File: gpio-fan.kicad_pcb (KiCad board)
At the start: 2 copper layers, 36 x 21.7 mm, 26 parts, among them J1 Conn_01x05, J2 Conn_01x05, J3 Conn_01x02, J4 Conn_02x07_Odd_Even, J5 Conn_01x03, J6 Conn_01x02, J7 Conn_01x02, J8 Conn_01x02, Q1 BSS214NW, SW1 SW_DIP_x03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

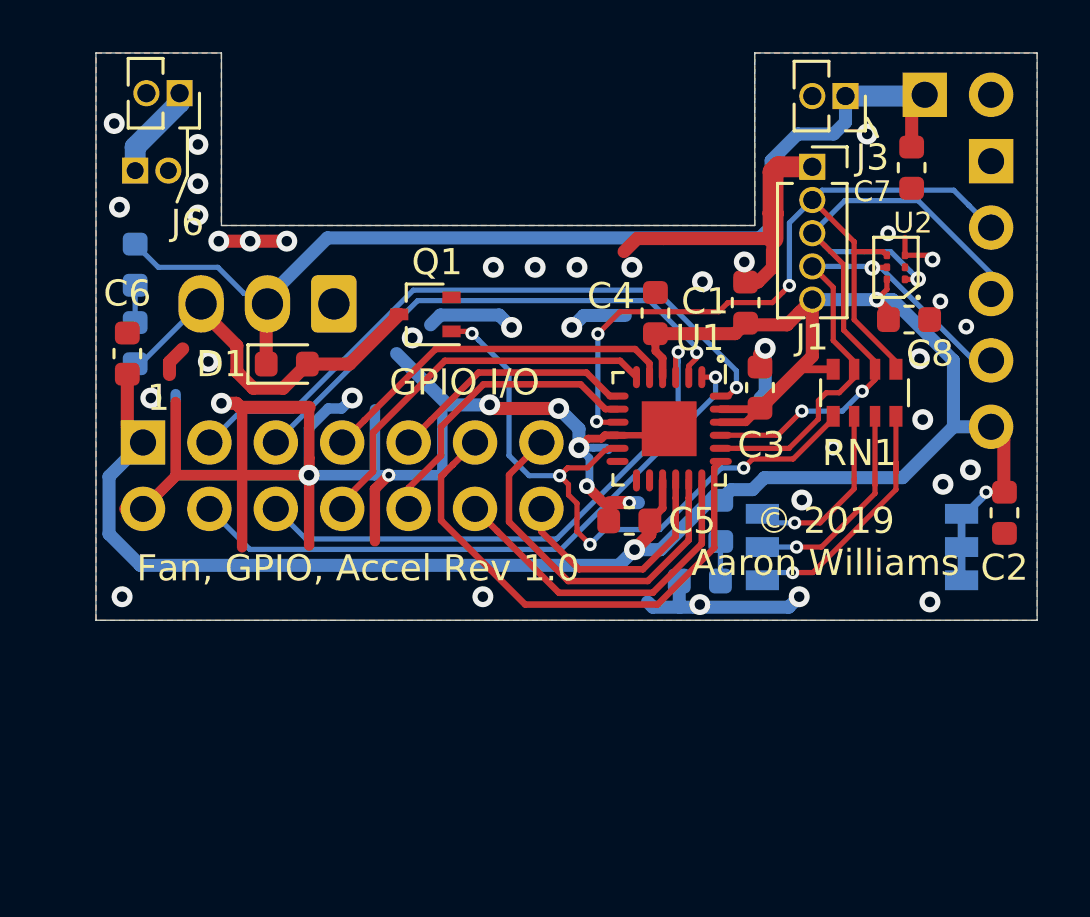
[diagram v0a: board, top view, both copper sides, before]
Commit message: Added large via to match 3.8, minor changes
Signed-off-by: Aaron Williams <aaron.w2@gmail.com>
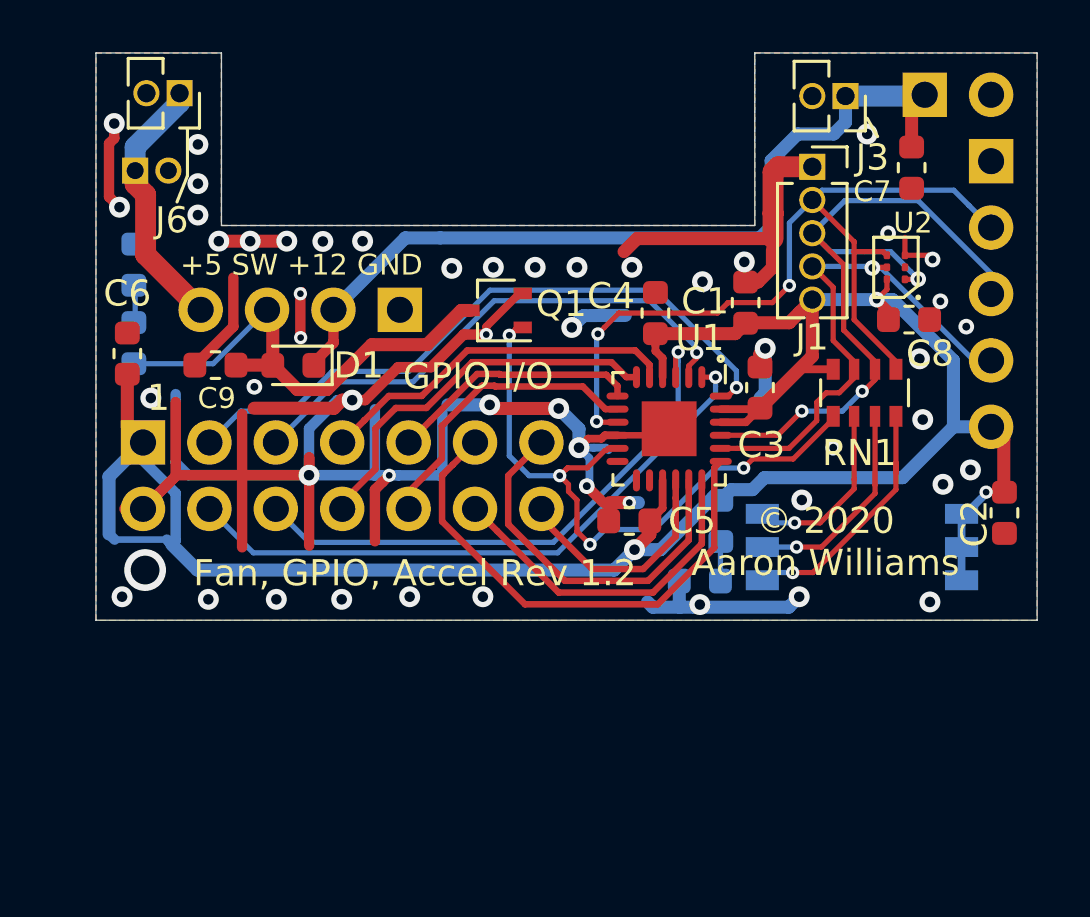
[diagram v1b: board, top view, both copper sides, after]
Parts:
- added C9: 1uF, Capacitor_SMD:C_0603_1608Metric, F.Cu at (54.6, 53.9)
- J5: value Conn_01x03 -> Conn_01x04_Male; footprint Connector_Molex:Molex_KK-254_AE-6410-03A_1x03_P2.54mm_Vertical -> Connector_PinHeader_2.54mm:PinHeader_1x04_P2.54mm_Vertical
- R1: value 4.7K -> 1K
- moved Q1 2.73 mm to (65.3, 51.9)
- moved J5 2.54 mm to (61.6, 51.8), turned to 90 degrees
- moved D1 0.25 mm to (57.5, 54.0), turned to 180 degrees
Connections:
- R1 pad 1: +12V -> +5V
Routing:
- net +5V: track 3.66 -> 13.7 mm
- net +12V: track 41.2 -> 33.0 mm
- net GND: track 105.3 -> 112.1 mm, vias 45 -> 53
- net +3V3: track 82.7 -> 87.3 mm
- net /FET: track 14.5 -> 18.8 mm
- net /FAN_CTL: track 25.5 -> 24.6 mm
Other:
- board text added: "+5 SW +12 GND"
- board text added: "Fan, GPIO, Accel Rev 1.2"
- board text added: "GND +12 SW +5"
- board text added: "J5: GND +12V FET +5"
- board text added: "© 2020 Aaron Williams"
- board text removed: "Fan, GPIO, Accel Rev 1.0"
- board text removed: "J5: GND +12V FET"
- board text removed: "© 2019 Aaron Williams"

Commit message: Upgraded to revision 1.3, changed temperature sensor and accelerometer.
This now uses a combined part that should be a lot easier to solder.
The new ST part also includes a temperature sensor and it is supported
by the Arduino library.

Signed-off-by: Aaron Williams <aaron.w2@gmail.com>
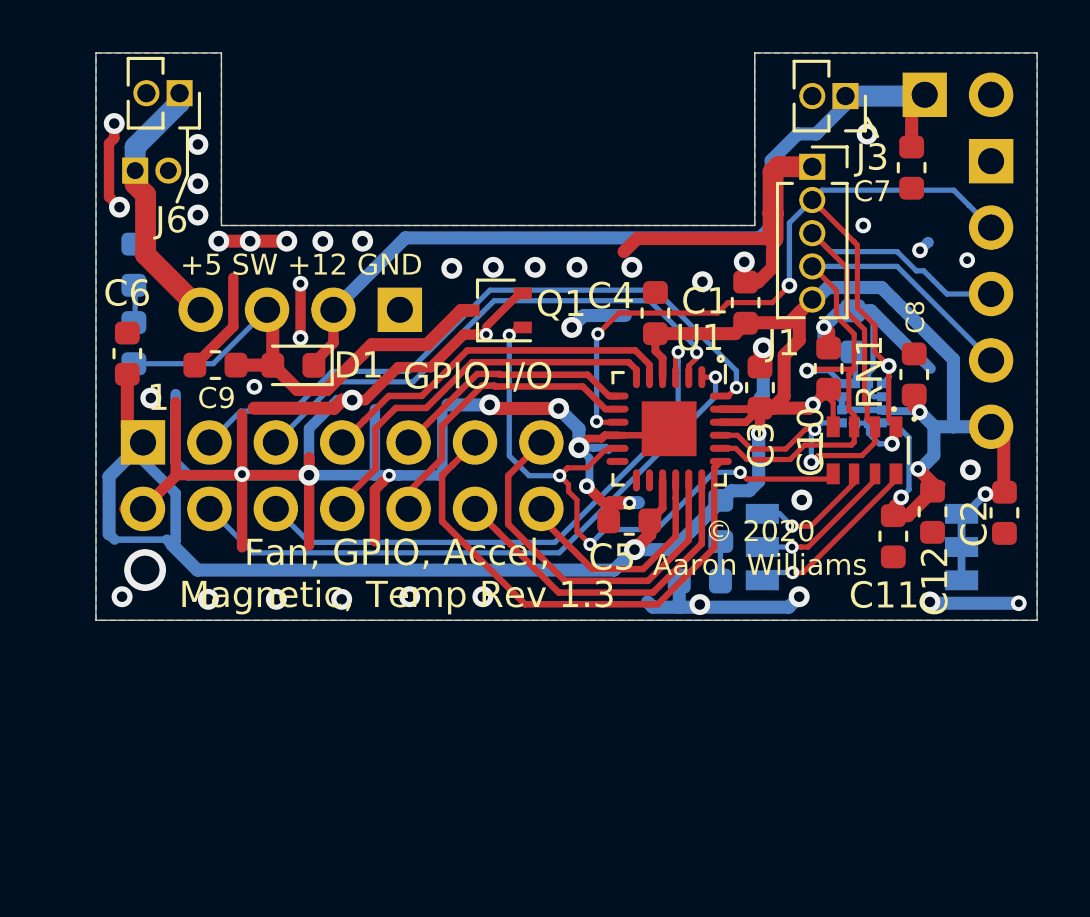
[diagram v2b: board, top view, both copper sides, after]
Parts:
- added C10: 0.22uF, Capacitor_SMD:C_0603_1608Metric, B.Cu at (79.0, 52.6)
- added C10: 0.01uF, Capacitor_SMD:C_0603_1608Metric, F.Cu at (78.0, 54.1)
- added C11: 0.1uF, Capacitor_SMD:C_0603_1608Metric, F.Cu at (80.5, 60.5)
- added C12: 10uF, Capacitor_SMD:C_0603_1608Metric, F.Cu at (82.0, 59.5)
- C8: value 1uF -> 0.1uF
- J2: value Conn_01x05 -> Conn_01x05 DNS
- J7, J8: value Conn_01x02 -> Conn_01x02 DNS
- U2: value MXC400XXC -> LSM303AGRTR; footprint Aaron:MXC400XXC -> Package_LGA:LGA-12_2x2mm_P0.5mm; moved to B.Cu
- moved U2 5.36 mm to (79.3, 55.4), turned to 0 degrees
- moved RN1 2.20 mm to (79.4, 57.2)
- moved C8 2.11 mm to (81.3, 54.3), turned to 90 degrees
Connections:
- U2 pad 2: Net-(U2-Pad2) -> +3V3
- U2 pad 3: GND -> +3V3
- U2 pad 4: /~INT -> /SDA
- U2 pad 5: /SDA -> Net-(C10-Pad1)
- U2 pad 6: +3V3 -> GND
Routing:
- net GND: track 112.1 -> 125.8 mm, vias 53 -> 51
- net +3V3: track 87.3 -> 99.0 mm, vias 3 -> 7
- net /SDA: track 20.4 -> 25.0 mm
- net /~INT: track 32.6 -> 37.0 mm, vias 3 -> 5
- net /~INT_PU: track 9.88 -> 6.93 mm
- net /SDA_PU: track 8.11 -> 5.61 mm
- net /SCL_PU: track 6.97 -> 4.74 mm
- net /SCL: track 28.0 -> 26.1 mm, vias 3 -> 2
- net Net-(C10-Pad1): track 0.00 -> 1.24 mm
- net /FAN_CTL: track 24.6 -> 23.9 mm
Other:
- board text added: "Fan, GPIO, Accel, Magnetic, Temp Rev 1.3"
- board text added: "GND ~INT~ SCL SDA 3"
- board text added: "I2C TERM"
- board text removed: "Fan, GPIO, Accel Rev 1.2"
- board text removed: "GND ~INT~ SCL SDA 3.3V"

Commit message: Fixed mislabeled capacitor and other minor changes.
Signed-off-by: Aaron Williams <aaron.w2@gmail.com>
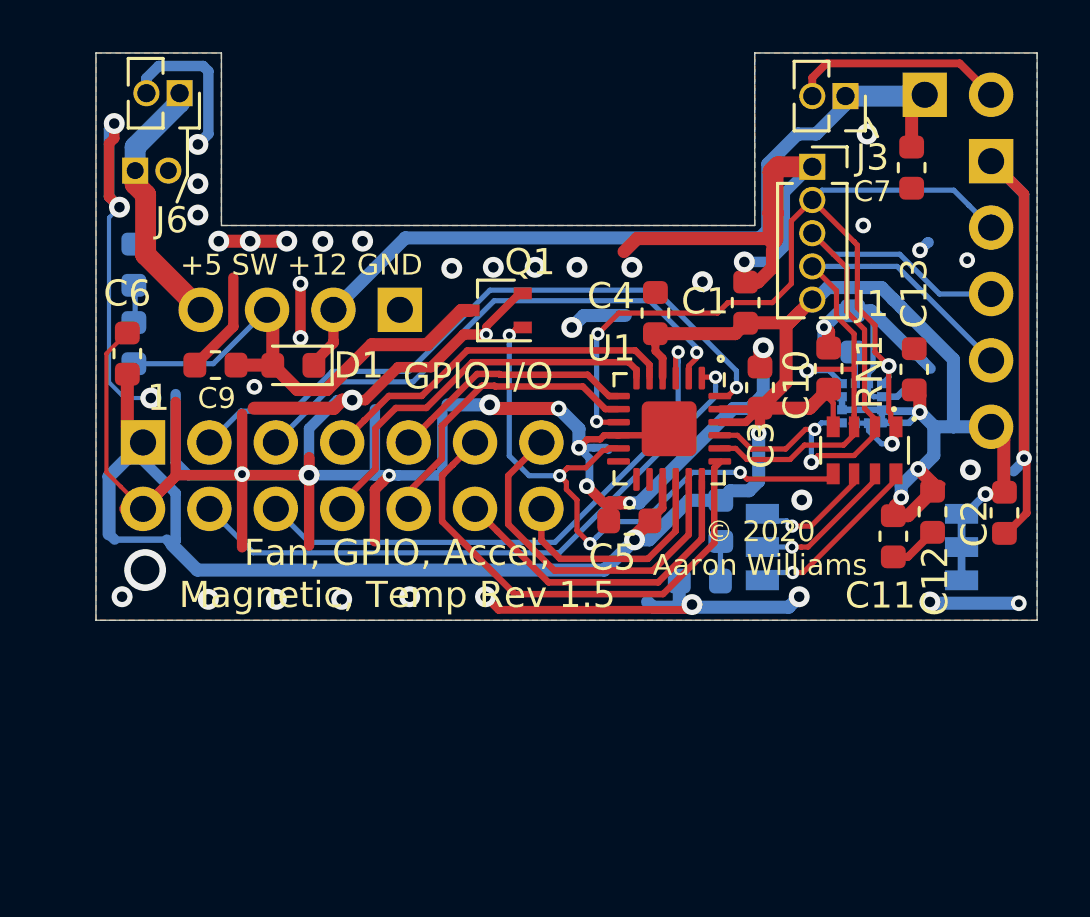
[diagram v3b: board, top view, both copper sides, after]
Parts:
- U1: footprint Aaron:HWQFN-24_EP_4x4_Pitch0.5mm -> Package_DFN_QFN:Texas_S-PVQFN-N24_EP2.1x2.1mm
- moved C13 0.20 mm to (81.3, 54.1)
- renumbered C8 to C13
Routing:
- net GND: track 125.8 -> 210.5 mm, vias 51 -> 52
- net +3V3: track 99.0 -> 98.4 mm, vias 7 -> 6
- net /~INT: vias 5 -> 4
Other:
- board text added: "Fan, GPIO, Accel, Magnetic, Temp Rev 1.5"
- board text removed: "Fan, GPIO, Accel, Magnetic, Temp Rev 1.3"

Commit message: Fixed J6, dimmed LEDs, and added ADC for light sensor
This also expands the board size where the switches are so that it can be
better mounted to the main board via the +5V pins near the speaker connector.

Signed-off-by: Aaron Williams <aaron.w2@gmail.com>
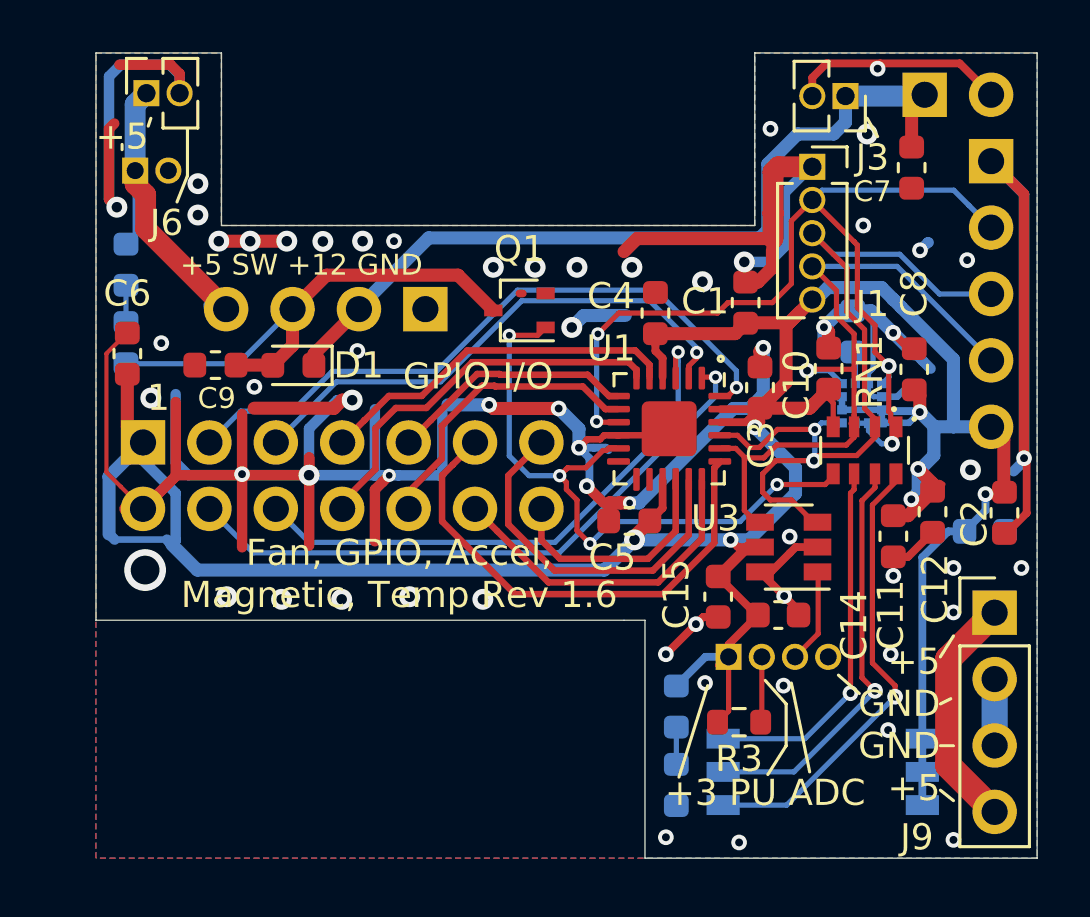
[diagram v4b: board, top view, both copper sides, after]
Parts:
- added C13: 0.1uF, Capacitor_SMD:C_0603_1608Metric, B.Cu at (84.0, 60.3)
- added C14: 1uF, Capacitor_SMD:C_0603_1608Metric, F.Cu at (76.1, 63.5)
- added C15: 0.1uF, Capacitor_SMD:C_0603_1608Metric, F.Cu at (73.8, 62.8)
- added J10: Conn_01x04 DNS, Connector_PinHeader_1.27mm:PinHeader_1x04_P1.27mm_Vertical, B.Cu at (74.2, 65.1)
- added J9: Conn_01x04 DNS, Connector_PinHeader_2.54mm:PinHeader_1x04_P2.54mm_Vertical, F.Cu at (84.4, 63.4)
- added R3: 4.7K, Resistor_SMD:R_0603_1608Metric, F.Cu at (74.6, 67.6)
- added U3: ADS1110, Package_TO_SOT_SMD:SOT-23-6, F.Cu at (76.5, 60.9)
- J5: value Conn_01x04_Male -> Conn_01x04 DNS
- R2: value 33 -> 100
- moved SW1 8.73 mm to (77.8, 69.5)
- moved D3 7.85 mm to (72.2, 70.0), turned to 90 degrees
- moved R2 7.30 mm to (72.2, 67.0)
- moved J6 1.27 mm to (51.9, 43.5), turned to 90 degrees
- moved J5 0.98 mm to (62.6, 51.8)
- moved Q1 0.88 mm to (66.2, 51.9)
- moved D2 0.30 mm to (51.1, 53.1)
- moved R1 0.30 mm to (51.1, 50.1)
- renumbered C13 to C8
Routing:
- net GND: track 210.5 -> 182.3 mm, vias 52 -> 61
- net +3V3: track 98.4 -> 123.8 mm, vias 6 -> 7
- net /~INT_PU: track 6.93 -> 17.6 mm
- net /SDA_PU: track 5.61 -> 15.8 mm
- net /SCL_PU: track 4.74 -> 14.0 mm
- net Net-(J9-Pad1): track 0.00 -> 9.09 mm
- net /SCL: track 26.0 -> 31.2 mm
- net /ADC_IN: track 0.00 -> 3.63 mm
- net /SDA: track 24.7 -> 27.5 mm
- net /PU_OUT: track 0.00 -> 2.52 mm
- net /FET: track 18.8 -> 19.9 mm
- net +5V: track 13.7 -> 12.9 mm
- net /FAN_CTL: track 23.8 -> 24.6 mm
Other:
- board size 36 x 21.7 mm -> 36 x 30.8 mm
- board text added: "+3 PU ADC"
- board text added: "+3 PU ADC GND"
- board text added: "+5"
- board text added: "+5 GND GND +5"
- board text added: "3 G"
- board text added: "Fan, GPIO, Accel, Magnetic, Temp Rev 1.6"
- board text removed: "Fan, GPIO, Accel, Magnetic, Temp Rev 1.5"

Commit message: Made minimum via hole size 0.3mm.
Signed-off-by: Aaron Williams <aaron.w2@gmail.com>
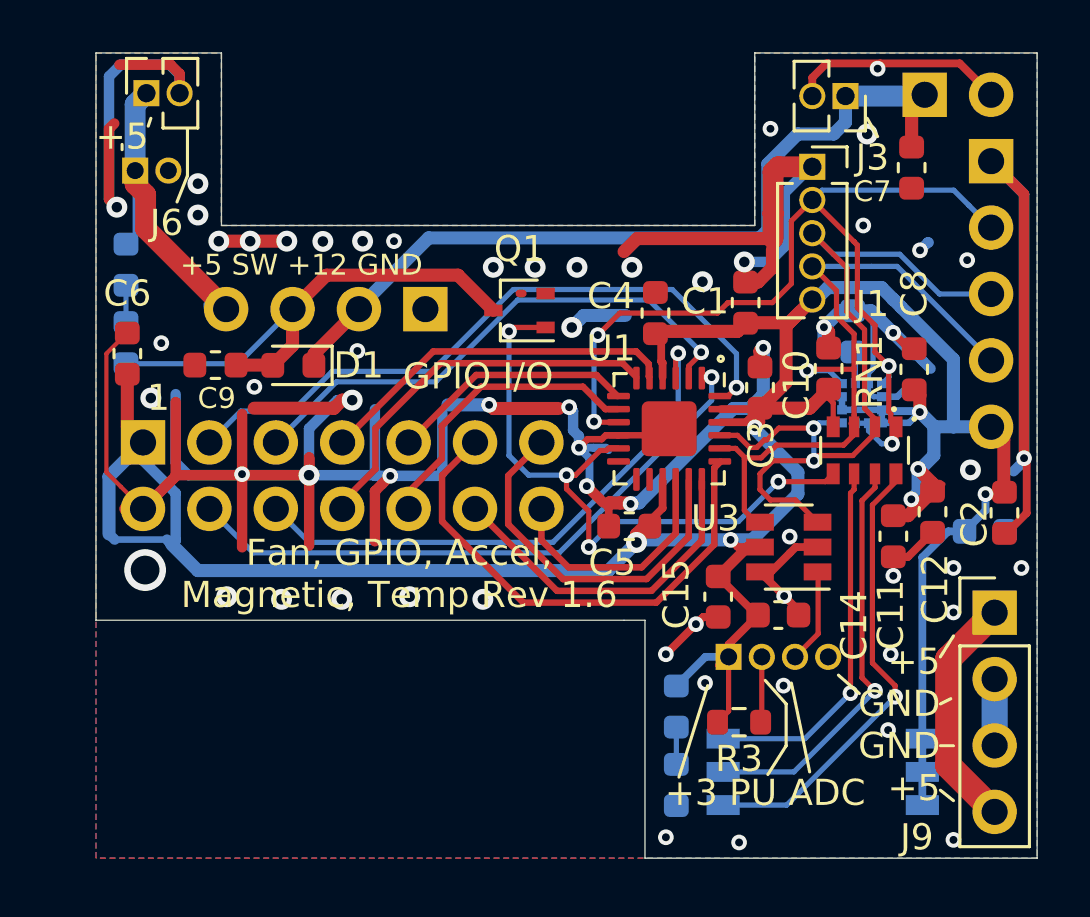
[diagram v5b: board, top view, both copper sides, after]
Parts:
- moved C5 0.20 mm to (70.4, 60.1)
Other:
- rule via_min_drill: 0.254 -> 0.3
- rule via_min_size: 0.508 -> 0.6
